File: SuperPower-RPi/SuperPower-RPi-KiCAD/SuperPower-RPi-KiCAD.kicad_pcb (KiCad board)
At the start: 2 copper layers, 65 x 56.5 mm, 118 parts, among them J1 Raspberry_Pi_2_3, J10 Conn_01x04, J11 QWIIC_Connector, J12 DNP, J13 Conn_01x06, J2 JST-PH, J3 Screw_Terminal_01x02, J4 Conn_01x02, J5 Conn_01x06, J6 USB_C_Receptacle_USB2.0, J7 Conn_01x03, J8 Conn_02x05_Odd_Even, J9 Conn_01x02, Q1 Q_PMOS_DMP3056L-7_SOT-23, Q2 Q_PMOS_DMP3056L-7_SOT-23, Q3 Q_PMOS_DMP3056L-7_SOT-23, Q6 2N7002-7-F, Q7 Q_PMOS_DMP3056L-7_SOT-23, SW1 Tact, U1 TPS61088, U2 BQ25895RTW, U3 STM32F412RETx, U4 ATtiny85-20SU, U5 ME6210A33M3G, U6 NCP380LMUAJAATBG

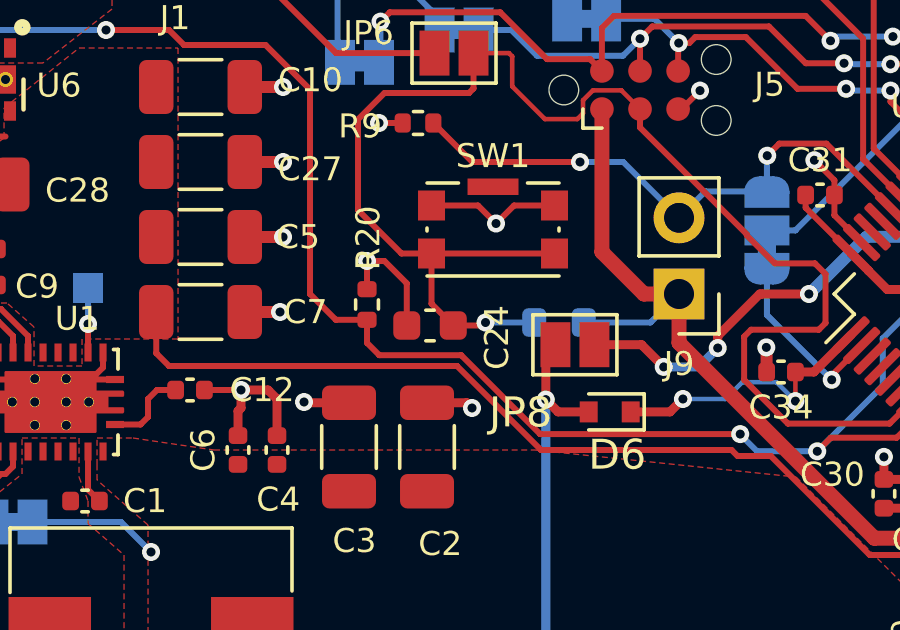
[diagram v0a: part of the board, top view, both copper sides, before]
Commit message: Changed C24 to 0402 to reduce unique parts/
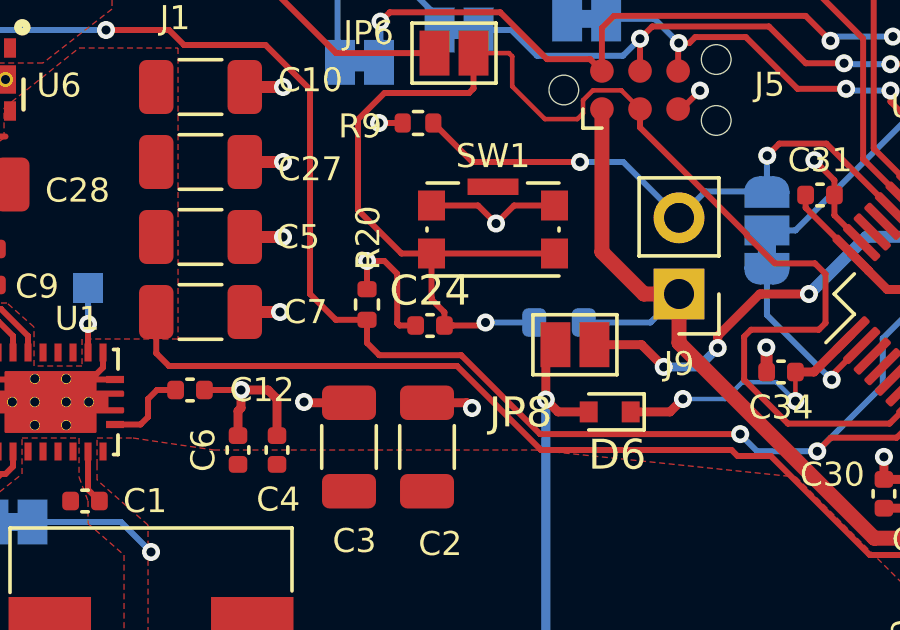
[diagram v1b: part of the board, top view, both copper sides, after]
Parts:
- C24: footprint Capacitor_SMD:C_0603_1608Metric -> Capacitor_SMD:C_0402_1005Metric

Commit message: Generated gerbers and position file.
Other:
- rule pad_to_mask_clearance: 0.051 -> 0

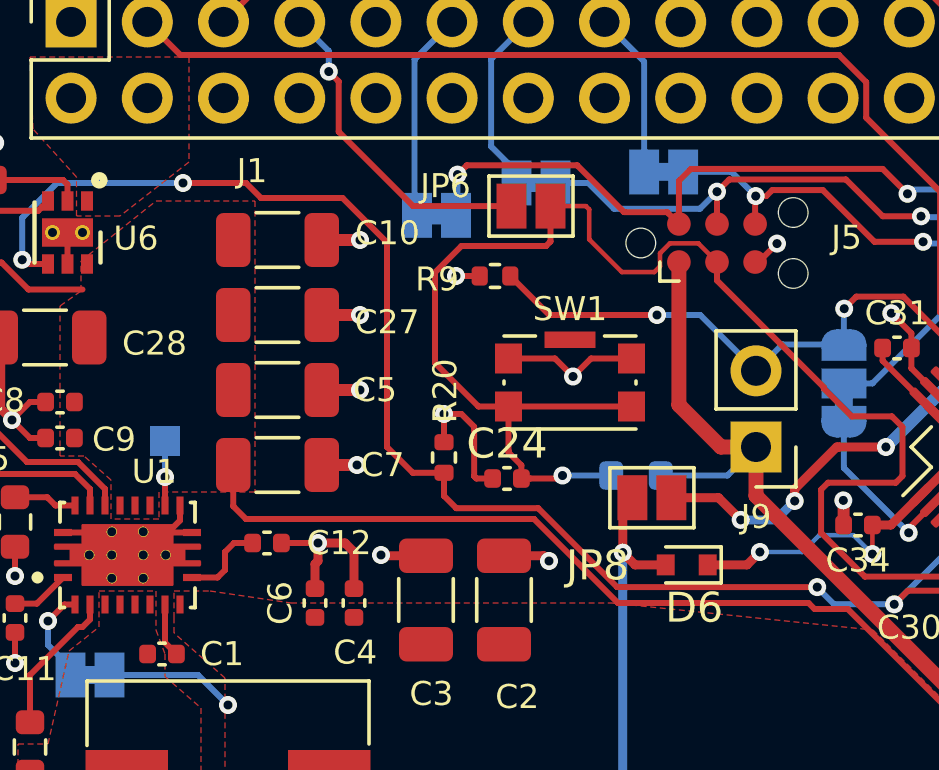
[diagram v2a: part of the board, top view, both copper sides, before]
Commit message: Changed Current Limit chip to Enable High, and changed the pull-up to connect to 3.3V
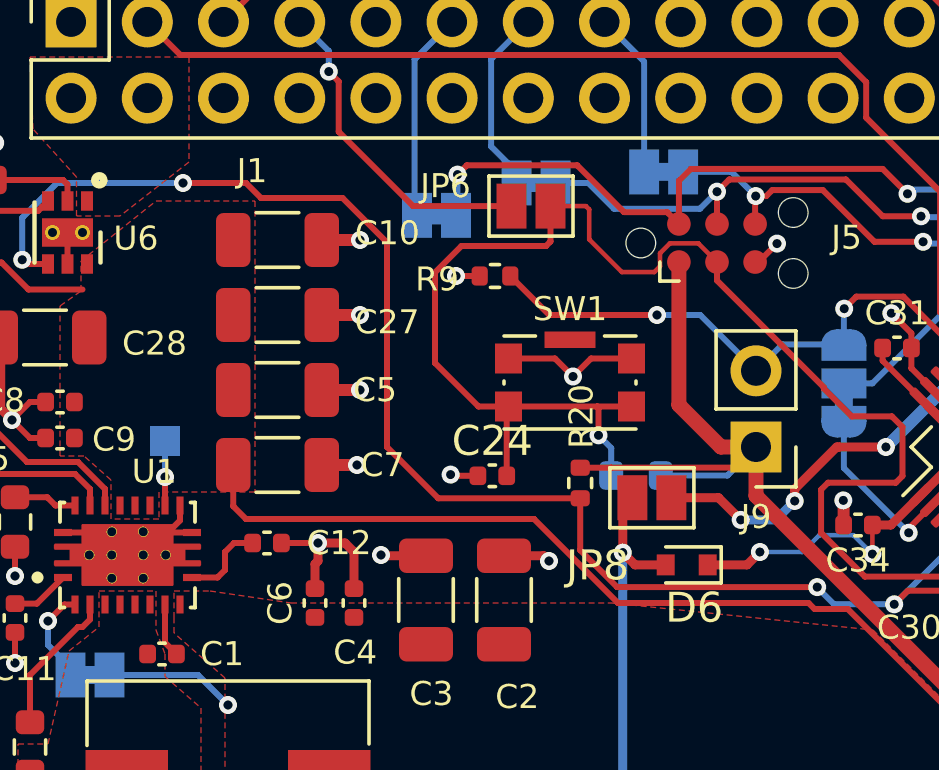
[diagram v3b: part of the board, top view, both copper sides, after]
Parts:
- J3: value Screw_Terminal_01x02 -> DNP
- J4: value Conn_01x02 -> DNP
- J5: value Conn_01x06 -> DNP
- JP1, JP7: value Jumper_3_Bridged12 -> DNP
- R19: value 5.23k -> DNP
- U6: value NCP380LMUAJAATBG -> NCP380HMU21AATBG
- moved R20 4.62 mm to (75.3, 68.1)
- moved C24 0.50 mm to (72.4, 67.9)
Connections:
- R20 pad 2: GND -> +3V3
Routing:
- net +3V3: track 137.6 -> 143.8 mm
- net GND: track 95.5 -> 92.0 mm
- net /Pi-MCU/nRESET: track 89.6 -> 88.8 mm
- net /Pi-MCU/GPIO0: track 53.2 -> 53.8 mm

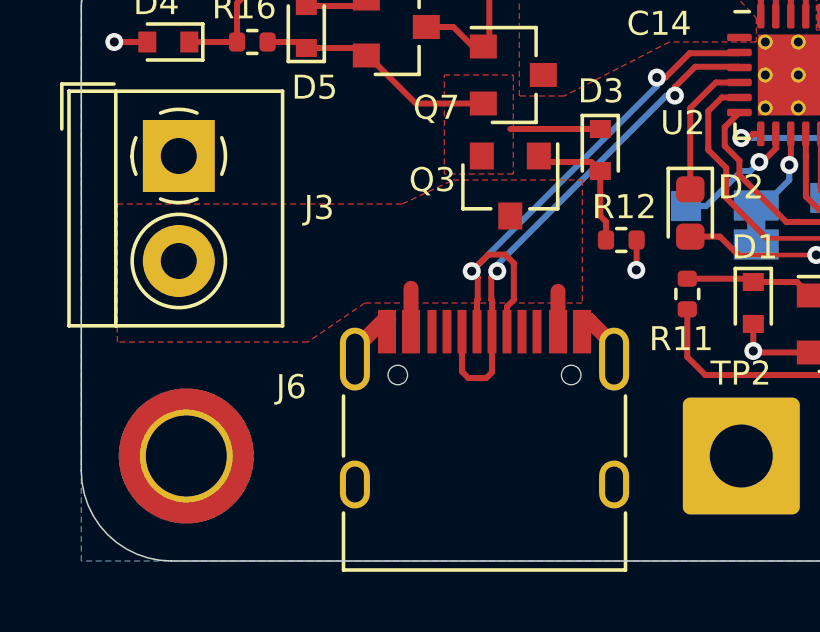
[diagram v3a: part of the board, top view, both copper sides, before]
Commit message: Added jumper to isolate the shield of the USB-C input power connector.
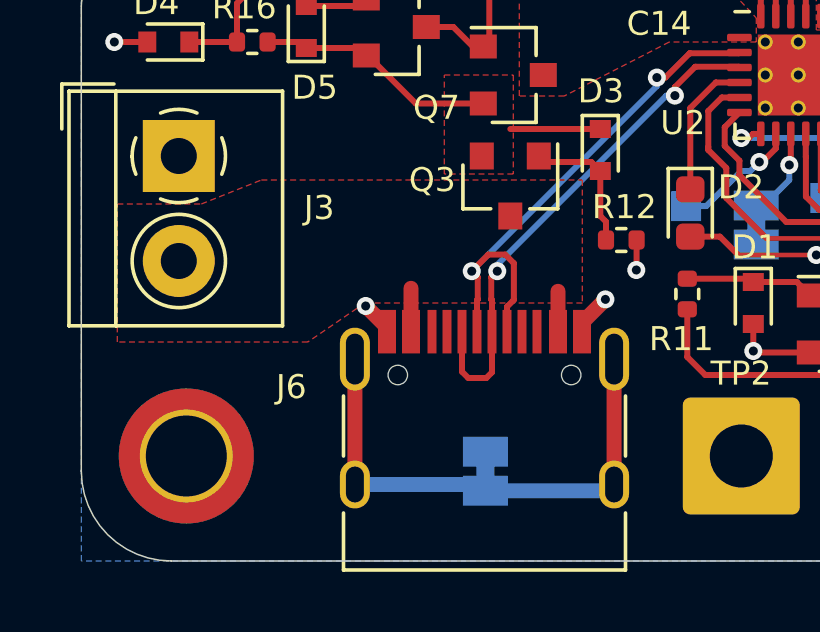
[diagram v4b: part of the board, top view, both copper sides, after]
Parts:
- added JP12: Jumper_NC_Small, Jumper:SolderJumper-2_P1.3mm_Bridged_Pad1.0x1.5mm, B.Cu at (63.5, 103.5)
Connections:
- J6 pad S1: GND -> Net-(J6-PadS1)
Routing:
- net Net-(J6-PadS1): track 0.00 -> 17.2 mm
- net GND: track 92.0 -> 91.7 mm, vias 40 -> 42
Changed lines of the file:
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@@
     (thickness 1.6)
     (drawings 40)
-    (tracks 1182)
+    (tracks 1190)
     (zones 0)
-    (modules 118)
-    (nets 138)
+    (modules 119)
+    (nets 139)
   )
   (page A4)
@@
   )
   (setup
-    (last_trace_width 0.2)
+    (last_trace_width 0.5)
     (user_trace_width 0.2)
     (user_trace_width 0.3)
@@
   (net 136 /SCL_RPi)
   (net 137 /SDA_RPi)
+  (net 138 "Net-(J6-PadS1)")
   (net_class Default "This is the default net class."
     (clearance 0.153)
@@
     (add_net "Net-(J6-PadB5)")
     (add_net "Net-(J6-PadB8)")
+    (add_net "Net-(J6-PadS1)")
     (add_net "Net-(J9-Pad2)")
     (add_net "Net-(JP3-Pad2)")
@@
     (add_net "Net-(U4-Pad2)")
   )
+  (module Jumper:SolderJumper-2_P1.3mm_Bridged_Pad1.0x1.5mm (layer B.Cu)
+    (at 63.47 103.51 270)
+    (descr "SMD Solder Jumper, 1x1.5mm Pads, 0.3mm gap, bridged with 1 copper strip")
+    (tags "solder jumper open")
+    (attr virtual)
+    (fp_text reference JP12 (at 0 1.8 90) (layer B.SilkS)
+      (effects (font (size 1 1) (thickness 0.15)) (justify mirror))
+    )
+    (fp_text value Jumper_NC_Small (at 0 -1.9 90) (layer B.Fab)
+      (effects (font (size 1 1) (thickness 0.15)) (justify mirror))
+    )
+    (fp_line (start -1.4 -1) (end -1.4 1) (layer B.SilkS) (width 0.12))
+    (fp_line (start 1.4 -1) (end -1.4 -1) (layer B.SilkS) (width 0.12))
+    (fp_line (start 1.4 1) (end 1.4 -1) (layer B.SilkS) (width 0.12))
+    (fp_line (start -1.4 1) (end 1.4 1) (layer B.SilkS) (width 0.12))
+    (fp_line (start -1.65 1.25) (end 1.65 1.25) (layer B.CrtYd) (width 0.05))
+    (fp_line (start -1.65 1.25) (end -1.65 -1.25) (layer B.CrtYd) (width 0.05))
+    (fp_line (start 1.65 -1.25) (end 1.65 1.25) (layer B.CrtYd) (width 0.05))
+    (fp_line (start 1.65 -1.25) (end -1.65 -1.25) (layer B.CrtYd) (width 0.05))
+    (fp_poly (pts (xy -0.25 0.3) (xy 0.25 0.3) (xy 0.25 -0.3) (xy -0.25 -0.3)) (layer B.Cu) (width 0))
+    (pad 2 smd rect (at 0.65 0 270) (size 1 1.5) (layers B.Cu B.Mask)
+      (net 138 "Net-(J6-PadS1)"))
+    (pad 1 smd rect (at -0.65 0 270) (size 1 1.5) (layers B.Cu B.Mask)
+      (net 3 GND))
+  )
   (module Capacitor_SMD:C_0402_1005Metric (layer F.Cu)
     (at 72.41 67.86)
@@
       (net 49 /Pi-Charger/D+))
     (pad S1 thru_hole oval (at 4.32 -3.13) (size 1 2.1) (drill oval 0.6 1.7) (layers *.Cu *.Mask)
-      (net 3 GND))
+      (net 138 "Net-(J6-PadS1)"))
     (pad S1 thru_hole oval (at -4.32 -3.13) (size 1 2.1) (drill oval 0.6 1.7) (layers *.Cu *.Mask)
-      (net 3 GND))
+      (net 138 "Net-(J6-PadS1)"))
     (pad "" np_thru_hole circle (at -2.89 -2.6) (size 0.65 0.65) (drill 0.65) (layers *.Cu *.Mask))
     (pad S1 thru_hole oval (at -4.32 1.05) (size 1 1.6) (drill oval 0.6 1.2) (layers *.Cu *.Mask)
-      (net 3 GND))
+      (net 138 "Net-(J6-PadS1)"))
     (pad "" np_thru_hole circle (at 2.89 -2.6) (size 0.65 0.65) (drill 0.65) (layers *.Cu *.Mask))
     (pad S1 thru_hole oval (at 4.32 1.05) (size 1 1.6) (drill oval 0.6 1.2) (layers *.Cu *.Mask)
-      (net 3 GND))
+      (net 138 "Net-(J6-PadS1)"))
     (model ${KISYS3DMOD}/Connector_USB.3dshapes/USB_C_Receptacle_HRO_TYPE-C-31-M-12.wrl
       (at (xyz 0 0 0))
@@
   (segment (start 61.5 73.42) (end 61.88 73.8) (width 0.2) (layer F.Cu) (net 2))
   (segment (start 61.5 72.15) (end 61.5 73.42) (width 0.2) (layer F.Cu) (net 2))
-  (segment (start 60.095 98.455) (end 59.18 99.37) (width 0.5) (layer F.Cu) (net 3))
-  (segment (start 60.25 98.455) (end 60.095 98.455) (width 0.5) (layer F.Cu) (net 3))
   (segment (start 61 69.75) (end 60.25 70.5) (width 0.2) (layer F.Cu) (net 3))
   (segment (start 62.4 69.75) (end 61 69.75) (width 0.2) (layer F.Cu) (net 3))
@@
   (segment (start 72.9 84.025) (end 71.525 84.025) (width 0.2) (layer F.Cu) (net 3))
   (segment (start 71.525 84.025) (end 71.5 84) (width 0.2) (layer F.Cu) (net 3))
-  (segment (start 66.75 98.455) (end 66.905 98.455) (width 0.5) (layer F.Cu) (net 3))
   (segment (start 68.51 95.8) (end 68.51 96.79) (width 0.2) (layer F.Cu) (net 3))
   (segment (start 68.51 96.79) (end 68.5 96.8) (width 0.2) (layer F.Cu) (net 3))
-  (segment (start 66.905 98.455) (end 67.82 99.37) (width 0.5) (layer F.Cu) (net 3))
   (segment (start 75.8625 89.05) (end 76.75 89.05) (width 0.3) (layer F.Cu) (net 3))
   (segment (start 75.8625 89.55) (end 76.75 89.55) (width 0.3) (layer F.Cu) (net 3))
@@
   (segment (start 71.06 67.86) (end 71.02 67.82) (width 0.2) (layer F.Cu) (net 3))
   (segment (start 71.93 67.86) (end 71.06 67.86) (width 0.2) (layer F.Cu) (net 3))
+  (via (at 67.47 97.78) (size 0.6) (drill 0.3) (layers F.Cu B.Cu) (net 3))
+  (segment (start 66.69 98.56) (end 67.47 97.78) (width 0.5) (layer F.Cu) (net 3))
+  (segment (start 66.69 98.855) (end 66.69 98.56) (width 0.5) (layer F.Cu) (net 3))
+  (via (at 59.48 98) (size 0.6) (drill 0.3) (layers F.Cu B.Cu) (net 3))
+  (segment (start 60.19 98.71) (end 59.48 98) (width 0.5) (layer F.Cu) (net 3))
+  (segment (start 60.19 98.855) (end 60.19 98.71) (width 0.5) (layer F.Cu) (net 3))
   (segment (start 57.23 72.12) (end 58.1 71.25) (width 0.2) (layer F.Cu) (net 4))
   (segment (start 56.5 72.12) (end 57.23 72.12) (width 0.2) (layer F.Cu) (net 4))
@@
   (segment (start 103.997 66.747) (end 103.941 66.747) (width 0.153) (layer F.Cu) (net 137))
   (segment (start 103.447 66.253) (end 103.447 65.933338) (width 0.153) (layer F.Cu) (net 137))
+  (segment (start 59.12 99.77) (end 59.12 103.95) (width 0.5) (layer F.Cu) (net 138))
+  (segment (start 67.76 103.95) (end 67.76 99.77) (width 0.5) (layer F.Cu) (net 138))
+  (segment (start 63.26 103.95) (end 63.47 104.16) (width 0.5) (layer B.Cu) (net 138))
+  (segment (start 59.12 103.95) (end 63.26 103.95) (width 0.5) (layer B.Cu) (net 138))
+  (segment (start 67.55 104.16) (end 67.76 103.95) (width 0.5) (layer B.Cu) (net 138))
+  (segment (start 63.47 104.16) (end 67.55 104.16) (width 0.5) (layer B.Cu) (net 138))
   (zone (net 41) (net_name "Net-(J3-Pad2)") (layer F.Cu) (hatch edge 0.508)
     (connect_pads (clearance 0.2))
@@
       (pts
         (xy 66.7 97.9) (xy 59.45 97.9) (xy 57.55 99.2) (xy 51.2 99.2) (xy 51.2 94.6)
-        (xy 60.7 94.6) (xy 62.4 93.8) (xy 66.7 93.8)
+        (xy 54 94.6) (xy 56 93.8) (xy 66.7 93.8)
       )
     )
